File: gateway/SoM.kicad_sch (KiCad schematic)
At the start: 26 parts, among them Q1001 BSS123, SW1001 Reset, SW1002 On / Off, X1001 UART, X1002 SoM

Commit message: Working on layout
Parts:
- BT1001: footprint (none) -> Keystone:3034; manf (none) -> Keystone Electronics; manf# (none) -> 3034; mouser# (none) -> 534-3034
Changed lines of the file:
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@@
 			)
 		)
-		(property "Footprint" ""
+		(property "Footprint" "Keystone:3034"
 			(at 215.9 167.386 90)
 			(hide yes)
@@
 			)
 		)
-		(property "Datasheet" ""
+		(property "Datasheet" "https://www.mouser.de/datasheet/3/201/1/3034.pdf"
 			(at 215.9 167.386 90)
 			(hide yes)
@@
 			)
 		)
-		(property "manf" ""
+		(property "manf" "Keystone Electronics"
 			(at 215.9 168.91 0)
 			(hide yes)
@@
 			)
 		)
-		(property "manf#" ""
+		(property "manf#" "3034"
 			(at 215.9 168.91 0)
 			(hide yes)
@@
 			)
 		)
-		(property "mouser#" ""
+		(property "mouser#" "534-3034"
 			(at 215.9 168.91 0)
 			(hide yes)

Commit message: Working on layout
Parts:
- removed TP1001, TP1002: ~, Testpoints_Kampi:TestPoint_Pad_1.0x1.0mm, symbol Connector:TestPoint
- added MP1001: (no value), Bivar:SLP3-300-100-F, symbol Mechanical_Kampi:Light_Pipe
- BT1001: footprint Keystone:3034 -> Keystone:3030TR; manf# 3034 -> 3030KTR; mouser# 534-3034 -> 534-3030KTR
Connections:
- net GPIO.Num0: now also X1002.21; no longer X1002.17
- net GPIO.Num2: now also X1002.17; no longer X1002.21
- net GPIO.Num3: now also X1002.96; no longer X1002.94
- net GPIO.Num4: now also X1002.94; no longer X1002.96
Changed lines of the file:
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@@
 	)
 	(junction
-		(at 241.3 163.83)
-		(diameter 0)
-		(color 0 0 0 0)
-	)
-	(junction
 		(at 50.8 156.21)
 		(diameter 0)
@@
 	)
 	(junction
+		(at 241.3 163.83)
+		(diameter 0)
+		(color 0 0 0 0)
+	)
+	(junction
 		(at 226.06 146.05)
 		(diameter 0)
@@
 		)
 	)
+	(wire
+		(pts
+			(xy 241.3 163.83) (xy 241.3 166.37)
+		)
+		(stroke
+			(width 0)
+			(type default)
+		)
+	)
 	(bus
 		(pts
@@
 	(wire
 		(pts
+			(xy 241.3 163.83) (xy 242.57 163.83)
+		)
+		(stroke
+			(width 0)
+			(type default)
+		)
+	)
+	(wire
+		(pts
 			(xy 147.32 151.13) (xy 148.59 151.13)
 		)
@@
 		)
 	)
-	(wire
-		(pts
-			(xy 142.24 265.43) (xy 142.24 266.7)
-		)
-		(stroke
-			(width 0)
-			(type default)
-		)
-	)
 	(bus
 		(pts
@@
 	(wire
 		(pts
-			(xy 241.3 163.83) (xy 241.3 161.29)
-		)
-		(stroke
-			(width 0)
-			(type default)
-		)
-	)
-	(wire
-		(pts
 			(xy 303.53 195.58) (xy 304.8 195.58)
 		)
@@
 	(wire
 		(pts
-			(xy 303.53 195.58) (xy 303.53 196.85)
-		)
-		(stroke
-			(width 0)
-			(type default)
-		)
-	)
-	(wire
-		(pts
 			(xy 173.99 189.23) (xy 194.31 189.23)
 		)
@@
 	(wire
 		(pts
-			(xy 241.3 163.83) (xy 241.3 166.37)
+			(xy 241.3 161.29) (xy 241.3 163.83)
 		)
 		(stroke
@@
 	(wire
 		(pts
-			(xy 242.57 163.83) (xy 241.3 163.83)
-		)
-		(stroke
-			(width 0)
-			(type default)
-		)
-	)
-	(wire
-		(pts
 			(xy 304.8 220.98) (xy 304.8 227.33)
 		)
@@
 	)
 	(label "GPIO.Num4"
-		(at 95.25 186.69 180)
+		(at 95.25 184.15 180)
 		(effects
 			(font
@@
 	)
 	(label "GPIO.Num2"
-		(at 39.37 92.71 0)
+		(at 39.37 87.63 0)
 		(effects
 			(font
@@
 	)
 	(label "GPIO.Num3"
-		(at 95.25 184.15 180)
+		(at 95.25 186.69 180)
 		(effects
 			(font
@@
 	)
 	(label "GPIO.Num0"
-		(at 39.37 87.63 0)
+		(at 39.37 92.71 0)
 		(effects
 			(font
@@
 	)
 	(symbol
-		(lib_id "Connector:TestPoint")
-		(at 142.24 265.43 0)
-		(mirror y)
-		(unit 1)
-		(body_style 1)
-		(exclude_from_sim no)
-		(in_bom no)
-		(on_board yes)
-		(in_pos_files no)
-		(dnp no)
-		(property "Reference" "TP1001"
-			(at 139.7 260.8579 0)
-			(show_name no)
-			(do_not_autoplace no)
-			(effects
-				(font
-					(size 1.27 1.27)
-				)
-				(justify left)
-			)
-		)
-		(property "Value" "~"
-			(at 139.7 263.3979 0)
-			(show_name no)
-			(do_not_autoplace no)
-			(effects
-				(font
-					(size 1.27 1.27)
-				)
-				(justify left)
-			)
-		)
-		(property "Footprint" "Testpoints_Kampi:TestPoint_Pad_1.0x1.0mm"
-			(at 137.16 265.43 0)
-			(hide yes)
-			(show_name no)
-			(do_not_autoplace no)
-			(effects
-				(font
-					(size 1.27 1.27)
-				)
-			)
-		)
-		(property "Datasheet" ""
-			(at 137.16 265.43 0)
-			(hide yes)
-			(show_name no)
-			(do_not_autoplace no)
-			(effects
-				(font
-					(size 1.27 1.27)
-				)
-			)
-		)
-		(property "Description" "test point"
-			(at 142.24 265.43 0)
-			(hide yes)
-			(show_name no)
-			(do_not_autoplace no)
-			(effects
-				(font
-					(size 1.27 1.27)
-				)
-			)
-		)
-		(property "manf" ""
-			(at 142.24 265.43 0)
-			(hide yes)
-			(show_name no)
-			(do_not_autoplace no)
-			(effects
-				(font
-					(size 1.27 1.27)
-				)
-			)
-		)
-		(property "manf#" ""
-			(at 142.24 265.43 0)
-			(hide yes)
-			(show_name no)
-			(do_not_autoplace no)
-			(effects
-				(font
-					(size 1.27 1.27)
-				)
-			)
-		)
-		(property "mouser#" ""
-			(at 142.24 265.43 0)
-			(hide yes)
-			(show_name no)
-			(do_not_autoplace no)
-			(effects
-				(font
-					(size 1.27 1.27)
-				)
-			)
-		)
-		(pin "1"
-		)
-		(instances
-			(project "Gateway"
-				(path "/d5742f03-3b1a-42e5-a384-018bd4b919aa/c5103ceb-5325-4a84-a025-9638a412984e/e744f3ce-03a6-44a6-8792-1447ef232b9a"
-					(reference "TP1001")
-					(unit 1)
-				)
-			)
-		)
-	)
-	(symbol
 		(lib_id "Device:R")
 		(at 314.96 158.75 180)
@@
 	)
 	(symbol
-		(lib_id "Connector:TestPoint")
-		(at 303.53 196.85 180)
+		(lib_id "Mechanical_Kampi:Light_Pipe")
+		(at 172.72 278.13 0)
 		(unit 1)
 		(body_style 1)
 		(exclude_from_sim no)
-		(in_bom no)
+		(in_bom yes)
 		(on_board yes)
 		(in_pos_files no)
 		(dnp no)
-		(fields_autoplaced yes)
-		(property "Reference" "TP1002"
-			(at 306.07 198.8819 0)
+		(property "Reference" "MP1001"
+			(at 169.164 275.59 0)
 			(show_name no)
 			(do_not_autoplace no)
@@
 					(size 1.27 1.27)
 				)
-				(justify right)
+				(justify left)
 			)
 		)
-		(property "Value" "~"
-			(at 306.07 201.4219 0)
+		(property "Value" ""
+			(at 172.72 278.13 0)
 			(show_name no)
 			(do_not_autoplace no)
@@
 					(size 1.27 1.27)
 				)
-				(justify right)
 			)
 		)
-		(property "Footprint" "Testpoints_Kampi:TestPoint_Pad_1.0x1.0mm"
-			(at 298.45 196.85 0)
+		(property "Footprint" "Bivar:SLP3-300-100-F"
+			(at 172.72 278.13 0)
 			(hide yes)
 			(show_name no)
@@
 			)
 		)
-		(property "Datasheet" ""
-			(at 298.45 196.85 0)
+		(property "Datasheet" "https://www.mouser.de/datasheet/3/112/1/SLP3_XXX_XXX_X.pdf"
+			(at 172.72 278.13 0)
 			(hide yes)
 			(show_name no)
@@
 			)
 		)
-		(property "Description" "test point"
-			(at 303.53 196.85 0)
+		(property "Description" ""
+			(at 172.72 278.13 0)
 			(hide yes)
 			(show_name no)
@@
 			)
 		)
-		(property "manf" ""
-			(at 303.53 196.85 0)
+		(property "manf" "Bivar"
+			(at 172.72 278.13 0)
 			(hide yes)
 			(show_name no)
@@
 			)
 		)
-		(property "manf#" ""
-			(at 303.53 196.85 0)
+		(property "manf#" "SLP3-300-100-F"
+			(at 172.72 278.13 0)
 			(hide yes)
 			(show_name no)
@@
 			)
 		)
-		(property "mouser#" ""
-			(at 303.53 196.85 0)
+		(property "mouser#" "749-SLP3-300-100-F"
+			(at 172.72 278.13 0)
 			(hide yes)
 			(show_name no)
@@
 			)
 		)
-		(pin "1"
-		)
 		(instances
 			(project "Gateway"
 				(path "/d5742f03-3b1a-42e5-a384-018bd4b919aa/c5103ceb-5325-4a84-a025-9638a412984e/e744f3ce-03a6-44a6-8792-1447ef232b9a"
-					(reference "TP1002")
+					(reference "MP1001")
 					(unit 1)
 				)
@@
 			)
 		)
-		(property "Footprint" "Keystone:3034"
+		(property "Footprint" "Keystone:3030TR"
 			(at 215.9 167.386 90)
 			(hide yes)
@@
 			)
 		)
-		(property "Datasheet" "https://www.mouser.de/datasheet/3/201/1/3034.pdf"
+		(property "Datasheet" "https://www.keyelco.com/product-pdf.cfm?p=14595"
 			(at 215.9 167.386 90)
 			(hide yes)
@@
 			)
 		)
-		(property "manf#" "3034"
+		(property "manf#" "3030KTR"
 			(at 215.9 168.91 0)
 			(hide yes)
@@
 			)
 		)
-		(property "mouser#" "534-3034"
+		(property "mouser#" "534-3030KTR"
 			(at 215.9 168.91 0)
 			(hide yes)

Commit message: Prepare release 1.0.0
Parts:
- removed R1003: 1k8, Resistor_SMD:R_0805_2012Metric, symbol Device:R
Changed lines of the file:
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@@
 	)
 	(junction
-		(at 109.22 125.73)
-		(diameter 0)
-		(color 0 0 0 0)
-	)
-	(junction
 		(at 50.8 100.33)
 		(diameter 0)
@@
 	(wire
 		(pts
-			(xy 109.22 125.73) (xy 110.49 125.73)
-		)
-		(stroke
-			(width 0)
-			(type default)
-		)
-	)
-	(wire
-		(pts
 			(xy 173.99 191.77) (xy 194.31 191.77)
 		)
@@
 	(wire
 		(pts
-			(xy 109.22 123.19) (xy 109.22 125.73)
-		)
-		(stroke
-			(width 0)
-			(type default)
-		)
-	)
-	(wire
-		(pts
 			(xy 27.94 273.05) (xy 31.75 273.05)
 		)
@@
 	(wire
 		(pts
-			(xy 109.22 115.57) (xy 109.22 114.3)
-		)
-		(stroke
-			(width 0)
-			(type default)
-		)
-	)
-	(wire
-		(pts
 			(xy 215.9 153.67) (xy 242.57 153.67)
 		)
@@
 	(wire
 		(pts
-			(xy 77.47 125.73) (xy 109.22 125.73)
+			(xy 77.47 125.73) (xy 110.49 125.73)
 		)
 		(stroke
@@
 	)
 	(symbol
-		(lib_id "Device:R")
-		(at 109.22 119.38 0)
-		(mirror y)
-		(unit 1)
-		(body_style 1)
-		(exclude_from_sim no)
-		(in_bom no)
-		(on_board yes)
-		(in_pos_files no)
-		(dnp yes)
-		(property "Reference" "R1003"
-			(at 111.76 118.1099 0)
-			(show_name no)
-			(do_not_autoplace no)
-			(effects
-				(font
-					(size 1.27 1.27)
-				)
-				(justify right)
-			)
-		)
-		(property "Value" "1k8"
-			(at 111.76 120.6499 0)
-			(show_name no)
-			(do_not_autoplace no)
-			(effects
-				(font
-					(size 1.27 1.27)
-				)
-				(justify right)
-			)
-		)
-		(property "Footprint" "Resistor_SMD:R_0805_2012Metric"
-			(at 110.998 119.38 90)
-			(hide yes)
-			(show_name no)
-			(do_not_autoplace no)
-			(effects
-				(font
-					(size 1.27 1.27)
-				)
-			)
-		)
-		(property "Datasheet" "https://www.mouser.de/datasheet/3/40/1/cr.pdf"
-			(at 109.22 119.38 0)
-			(hide yes)
-			(show_name no)
-			(do_not_autoplace no)
-			(effects
-				(font
-					(size 1.27 1.27)
-				)
-			)
-		)
-		(property "Description" "Resistor"
-			(at 109.22 119.38 0)
-			(hide yes)
-			(show_name no)
-			(do_not_autoplace no)
-			(effects
-				(font
-					(size 1.27 1.27)
-				)
-			)
-		)
-		(property "manf" "Bourns"
-			(at 109.22 119.38 0)
-			(hide yes)
-			(show_name no)
-			(do_not_autoplace no)
-			(effects
-				(font
-					(size 1.27 1.27)
-				)
-			)
-		)
-		(property "manf#" "CR0805-FX-1801GLF"
-			(at 109.22 119.38 0)
-			(hide yes)
-			(show_name no)
-			(do_not_autoplace no)
-			(effects
-				(font
-					(size 1.27 1.27)
-				)
-			)
-		)
-		(property "mouser#" "652-CR0805-FX-1801GLF"
-			(at 109.22 119.38 0)
-			(hide yes)
-			(show_name no)
-			(do_not_autoplace no)
-			(effects
-				(font
-					(size 1.27 1.27)
-				)
-			)
-		)
-		(pin "2"
-		)
-		(pin "1"
-		)
-		(instances
-			(project "Gateway"
-				(path "/d5742f03-3b1a-42e5-a384-018bd4b919aa/c5103ceb-5325-4a84-a025-9638a412984e/e744f3ce-03a6-44a6-8792-1447ef232b9a"
-					(reference "R1003")
-					(unit 1)
-				)
-			)
-		)
-	)
-	(symbol
 		(lib_id "power:GND")
 		(at 342.9 177.8 0)
@@
 					(unit 1)
 				)
-			)
-		)
-	)
-	(symbol
-		(lib_id "power:+1V8")
-		(at 109.22 114.3 0)
-		(mirror y)
-		(unit 1)
-		(body_style 1)
-		(exclude_from_sim no)
-		(in_bom yes)
-		(on_board yes)
-		(in_pos_files yes)
-		(dnp no)
-		(fields_autoplaced yes)
-		(property "Reference" "#PWR01004"
-			(at 109.22 118.11 0)
-			(hide yes)
-			(show_name no)
-			(do_not_autoplace no)
-			(effects
-				(font
-					(size 1.27 1.27)
-				)
-			)
-		)
-		(property "Value" "+1V8"
-			(at 109.22 109.22 0)
-			(show_name no)
-			(do_not_autoplace no)
-			(effects
-				(font
-					(size 1.27 1.27)
-				)
-			)
-		)
-		(property "Footprint" ""
-			(at 109.22 114.3 0)
-			(hide yes)
-			(show_name no)
-			(do_not_autoplace no)
-			(effects
-				(font
-					(size 1.27 1.27)
-				)
-			)
-		)
-		(property "Datasheet" ""
-			(at 109.22 114.3 0)
-			(hide yes)
-			(show_name no)
-			(do_not_autoplace no)
-			(effects
-				(font
-					(size 1.27 1.27)
-				)
-			)
-		)
-		(property "Description" "Power symbol creates a global label with name \"+1V8\""
-			(at 109.22 114.3 0)
-			(hide yes)
-			(show_name no)
-			(do_not_autoplace no)
-			(effects
-				(font
-					(size 1.27 1.27)
-				)
-			)
-		)
-		(pin "1"
-		)
-		(instances
-			(project "Gateway"
-				(path "/d5742f03-3b1a-42e5-a384-018bd4b919aa/c5103ceb-5325-4a84-a025-9638a412984e/e744f3ce-03a6-44a6-8792-1447ef232b9a"
-					(reference "#PWR01004")
-					(unit 1)
-				)

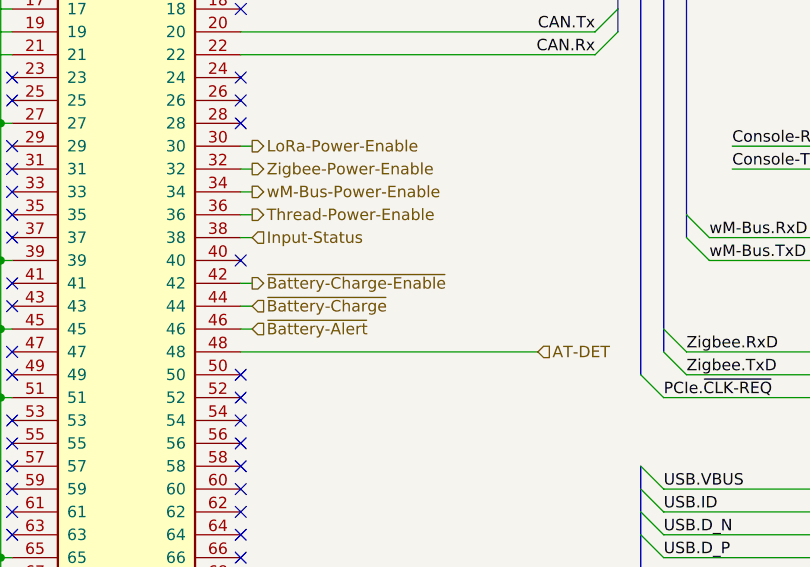
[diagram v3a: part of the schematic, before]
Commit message: Replace battery charger with BQ25300
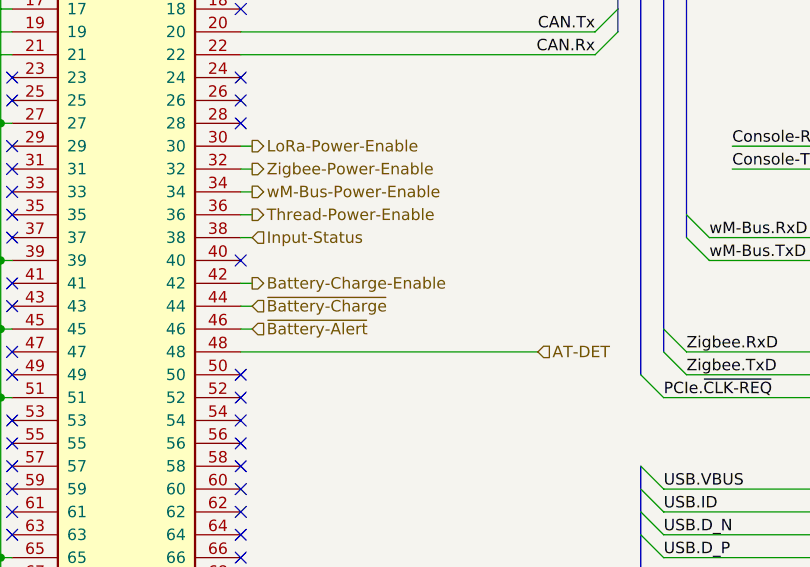
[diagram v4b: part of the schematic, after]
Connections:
- net ~{Battery-Charge-Enable} renamed Battery-Charge-Enable
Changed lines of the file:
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@@
 		)
 	)
-	(hierarchical_label "~{Battery-Charge-Enable}"
+	(hierarchical_label "Battery-Charge-Enable"
 		(shape output)
 		(at 78.74 118.11 0)

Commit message: Smaller changes
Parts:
- H1001, H1002: value MountingHole -> Spacer; symbol Mechanical_Kampi:MountingHole -> Mechanical:Spacer; now in the parts list
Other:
- moved on the sheet: LED1001, Q1001, R1004, R1005

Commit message: Working on revision 1.0.0
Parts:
- added H1003: MountingHole, MountingHole:MountingHole_3.2mm_M3_Pad_Via, symbol Misc:MountingHole_Pad
- C1001: symbol Device:C -> partdb:08055C104K4Z4A; Category (none) -> Kondensator/MLCC; MPN (none) -> 08055C104K4Z4A; Manufacturer (none) -> KYOCERA AVX; Manufacturing Status (none) -> Active; Mass (none) -> 0.006 g; Mouser SPN (none) -> 581-08055C104K4Z4A; Part-DB Footprint (none) -> 0805; Part-DB ID (none) -> 109; Part-DB URL (none) -> https://inventory.lan/de/part/109/info; Stock (none) -> 6; Storage Location (none) -> Sortierregal; manf# 08053C104M4T4A -> 08055C104K4Z4A; mouser# 581-08053C104M4T4A -> 581-08055C104K4Z4A
- H1001, H1002: footprint Wuerth:9774015151R -> Wuerth:9774025151R; symbol Mechanical:Spacer -> partdb:9774025151R; Category (none) -> Mechanik/Abstandshalter; MPN (none) -> 9774025151R; Manufacturer (none) -> Wurth Elektronik; Manufacturing Status (none) -> Active; Mass (none) -> 0.371 g; Mouser SPN (none) -> 710-9774025151R; Part-DB Footprint (none) -> WA-SMSI M2.5; Part-DB ID (none) -> 374; Part-DB URL (none) -> https://inventory.lan/de/part/374/info; Stock (none) -> 0; manf# 9774015151R -> 9774025151R; mouser# 710-9774015151R -> 710-9774025151R
- LED1001: symbol Device:LED -> partdb:SM0805YC; Category (none) -> Diode/LED/Gelb; MPN (none) -> SM0805YC; Manufacturer (none) -> Bivar; Manufacturing Status (none) -> Active; Mass (none) -> 0.004 g; Mouser SPN (none) -> 749-SM0805YC; Part-DB Footprint (none) -> 0805; Part-DB ID (none) -> 324; Part-DB URL (none) -> https://inventory.lan/de/part/324/info; Stock (none) -> 0
- MP1001: symbol Mechanical_Kampi:Light_Pipe -> Mechanical:Light_Pipe
- Q1001: value BSS123 -> BSS138; symbol Transistor_FET:BSS123 -> partdb:BSS138; Category (none) -> Transistor/N-Kanal; MPN (none) -> BSS138; Manufacturer (none) -> onsemi / Fairchild; Manufacturing Status (none) -> Active; Mass (none) -> 0.008 g; Mouser SPN (none) -> 512-BSS138; Part-DB Footprint (none) -> SOT-23-3; Part-DB ID (none) -> 353; Part-DB URL (none) -> https://inventory.lan/de/part/353/info; Stock (none) -> 0; manf onsemi -> onsemi / Fairchild; manf# BSS123 -> BSS138; mouser# 512-BSS123 -> 512-BSS138
- R1001, R1002, R1009: symbol Device:R -> partdb:CR0805-JW-182ELF; Category (none) -> Widerstand/Dickfilmwiderstand; MPN (none) -> CR0805-JW-182ELF; Manufacturer (none) -> Bourns; Manufacturing Status (none) -> Active; Mass (none) -> 0.0055 g; Mouser SPN (none) -> 652-CR0805JW-182ELF; Part-DB Footprint (none) -> 0805; Part-DB ID (none) -> 350; Part-DB URL (none) -> https://inventory.lan/de/part/350/info; Stock (none) -> 0; manf# CR0805-FX-1801GLF -> CR0805-JW-182ELF; mouser# 652-CR0805-FX-1801GLF -> 652-CR0805JW-182ELF
- R1004, R1008: symbol Device:R -> partdb:CR0805-FX-1002ELF; Category (none) -> Widerstand/Dickfilmwiderstand; MPN (none) -> CR0805-FX-1002ELF; Manufacturer (none) -> Bourns; Manufacturing Status (none) -> Active; Mass (none) -> 0.006 g; Mouser SPN (none) -> 652-CR0805FX-1002ELF; Part-DB Footprint (none) -> 0805; Part-DB ID (none) -> 343; Part-DB URL (none) -> https://inventory.lan/de/part/343/info; Stock (none) -> 0; manf# CR0805-JW-103GLF -> CR0805-FX-1002ELF; mouser# 652-CR0805-JW-103GLF -> 652-CR0805FX-1002ELF
- R1006, R1007, R1011: symbol Device:R -> partdb:CR0805-FX-1002ELF; Category (none) -> Widerstand/Dickfilmwiderstand; MPN (none) -> CR0805-FX-1002ELF; Manufacturer (none) -> Bourns; Manufacturing Status (none) -> Active; Mass (none) -> 0.006 g; Mouser SPN (none) -> 652-CR0805FX-1002ELF; Part-DB Footprint (none) -> 0805; Part-DB ID (none) -> 343; Part-DB URL (none) -> https://inventory.lan/de/part/343/info; Stock (none) -> 0; manf# CR0805-FX-1002GLF -> CR0805-FX-1002ELF; mouser# 652-CR0805-FX-1002GLF -> 652-CR0805FX-1002ELF
- R1013: symbol Device:R -> partdb:CR0805-J/-000ELF; Category (none) -> Widerstand/Dickfilmwiderstand; MPN (none) -> CR0805-J/-000ELF; Manufacturer (none) -> Bourns; Manufacturing Status (none) -> Active; Mass (none) -> 0.006 g; Mouser SPN (none) -> 652-CR0805-J/-000ELF; Part-DB Footprint (none) -> 0805; Part-DB ID (none) -> 322; Part-DB URL (none) -> https://inventory.lan/de/part/322/info; Stock (none) -> 0
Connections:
- net GND: now also H1003.1
- net Battery-Backup-Enable: now reaches X1002.114
- net Backup-Status renamed PowerMux-Status
- no-connect marks 151 -> 150
